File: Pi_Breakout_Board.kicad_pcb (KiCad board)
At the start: 2 copper layers, 56.5 x 65 mm, 74 parts, among them J1 Raspberry_Pi_2_3, J2 Conn_02x04_Odd_Even heater he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, J3 Conn_02x08_Odd_Even thermisto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, J4 Screw_Terminal_01x02, J5 Conn_01x08_Male, J6 Conn_01x08_Male, J7 Conn_01x02_Female, J8 Conn_01x03_Male, Q1 Q_NMOS_GDSD, Q2 Q_NMOS_GDSD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

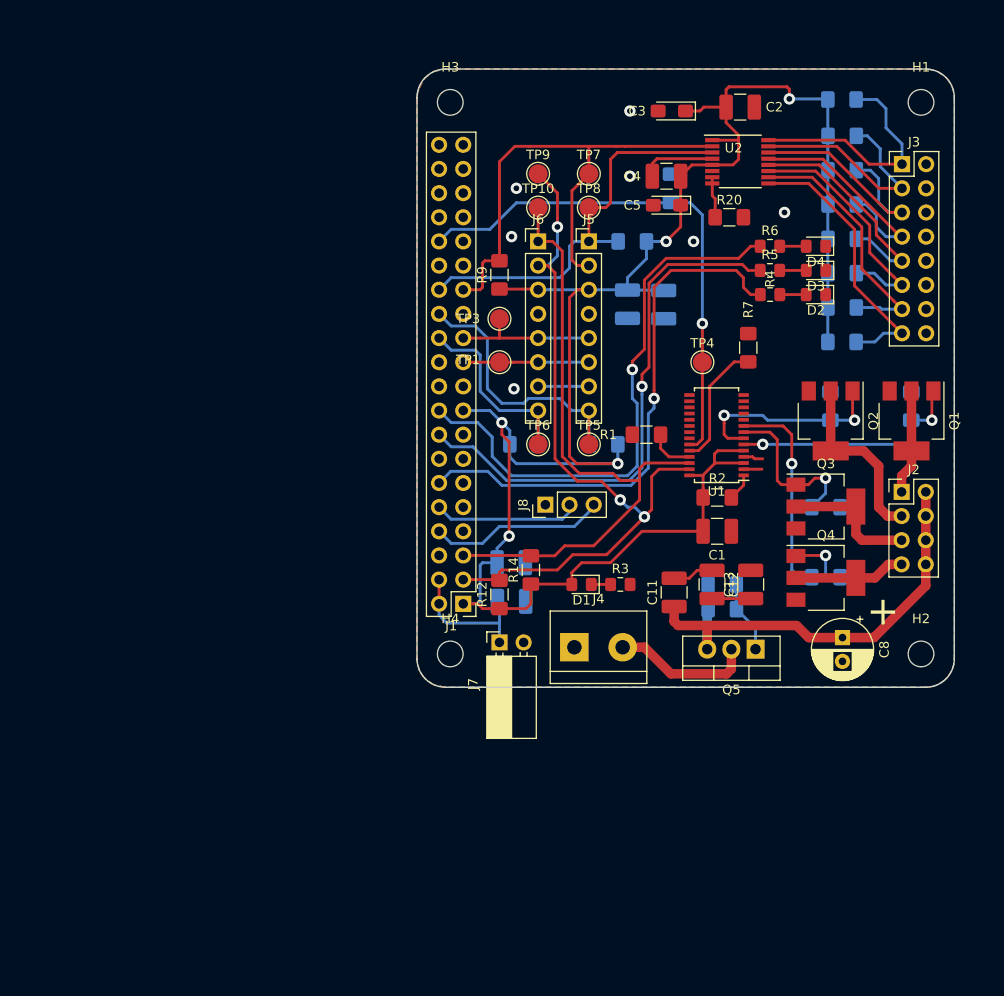
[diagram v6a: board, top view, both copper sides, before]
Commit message: Routing updates + double checks. Silkscreen
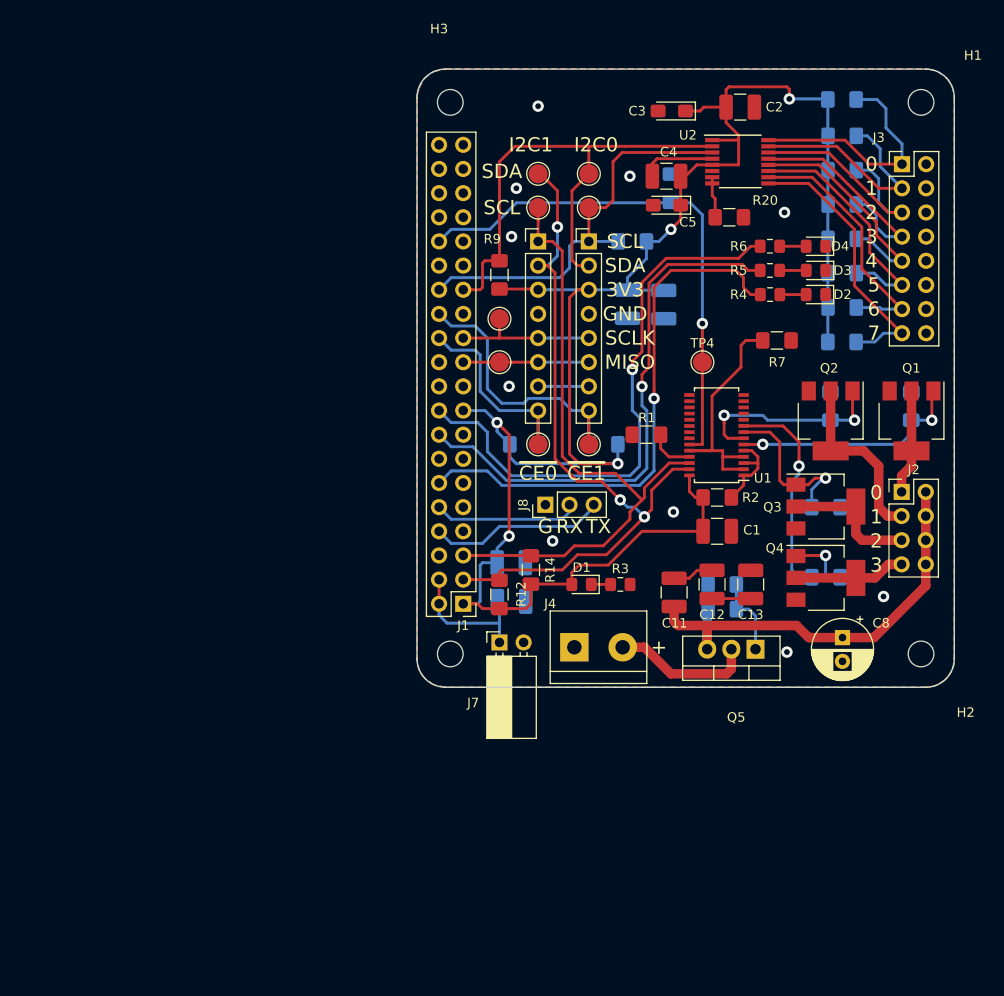
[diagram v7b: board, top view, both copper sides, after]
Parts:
- moved R7 3.11 mm to (87.8, 113.5), turned to 0 degrees
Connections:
- net Net-(J3-Pad1) renamed /ch0
- net Net-(J3-Pad11) renamed /ch5
- net Net-(J3-Pad13) renamed /ch6
- net Net-(J3-Pad15) renamed /ch7
- net Net-(J3-Pad3) renamed /ch1
- net Net-(J3-Pad5) renamed /ch2
- net Net-(J3-Pad7) renamed /ch3
- net Net-(J3-Pad9) renamed /ch4
- U1 pad 2: GND -> Net-(R7-Pad1)
- U1 pad 3: +3V3 -> Net-(R2-Pad1)
- U1 pad 4: GND -> Net-(R7-Pad1)
- U1 pad 5: +3V3 -> Net-(R2-Pad1)
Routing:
- net Net-(R7-Pad1): track 13.3 -> 27.1 mm
- net +3V3: track 209.7 -> 200.0 mm
- net Net-(R2-Pad1): track 2.86 -> 9.19 mm
- net GND: track 11.9 -> 7.85 mm, vias 7 -> 10
- net Net-(Q5-Pad1): track 7.64 -> 8.41 mm
- net LED_YELLOW: track 56.3 -> 57.1 mm
- net SDA1: track 76.7 -> 76.0 mm
- net Net-(Q4-Pad1): track 28.8 -> 29.4 mm
- net LED_GREEN: track 56.7 -> 57.3 mm
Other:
- board text added: "0"
- board text added: "1"
- board text added: "2"
- board text added: "3"
- board text added: "3V3"
- board text added: "4"
- board text added: "5"
- board text added: "6"
- board text added: "7"
- board text added: "G"
- board text added: "GND"
- board text added: "I2C0"
- board text added: "I2C1"
- board text added: "MISO"
- board text added: "RX"
- board text added: "SCL"
- board text added: "SCLK"
- board text added: "SDA"
- board text added: "TX"
- board text added: "~CE0"
- board text added: "~CE1"

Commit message: latest
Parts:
- moved C9 9.48 mm to (69.4, 137.4)
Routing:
- net +3V3: track 200.0 -> 176.6 mm, vias 5 -> 3
